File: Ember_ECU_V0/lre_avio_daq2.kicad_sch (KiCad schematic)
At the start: 64 parts, among them IC1 AS5600-ASOT, IC2 AS5600-ASOT, J1 Screw_Terminal_01x02, J2 Conn_01x04, U1 STM32F411CEUx, U2 HX711, U3 SN65HVD230, U4 MPXA6115A, U5 MPXA6115A, U6 MPXA6115A, U7 MAX31856, U8 MAX31856, U9 MAX31856, Y1 8 MHz

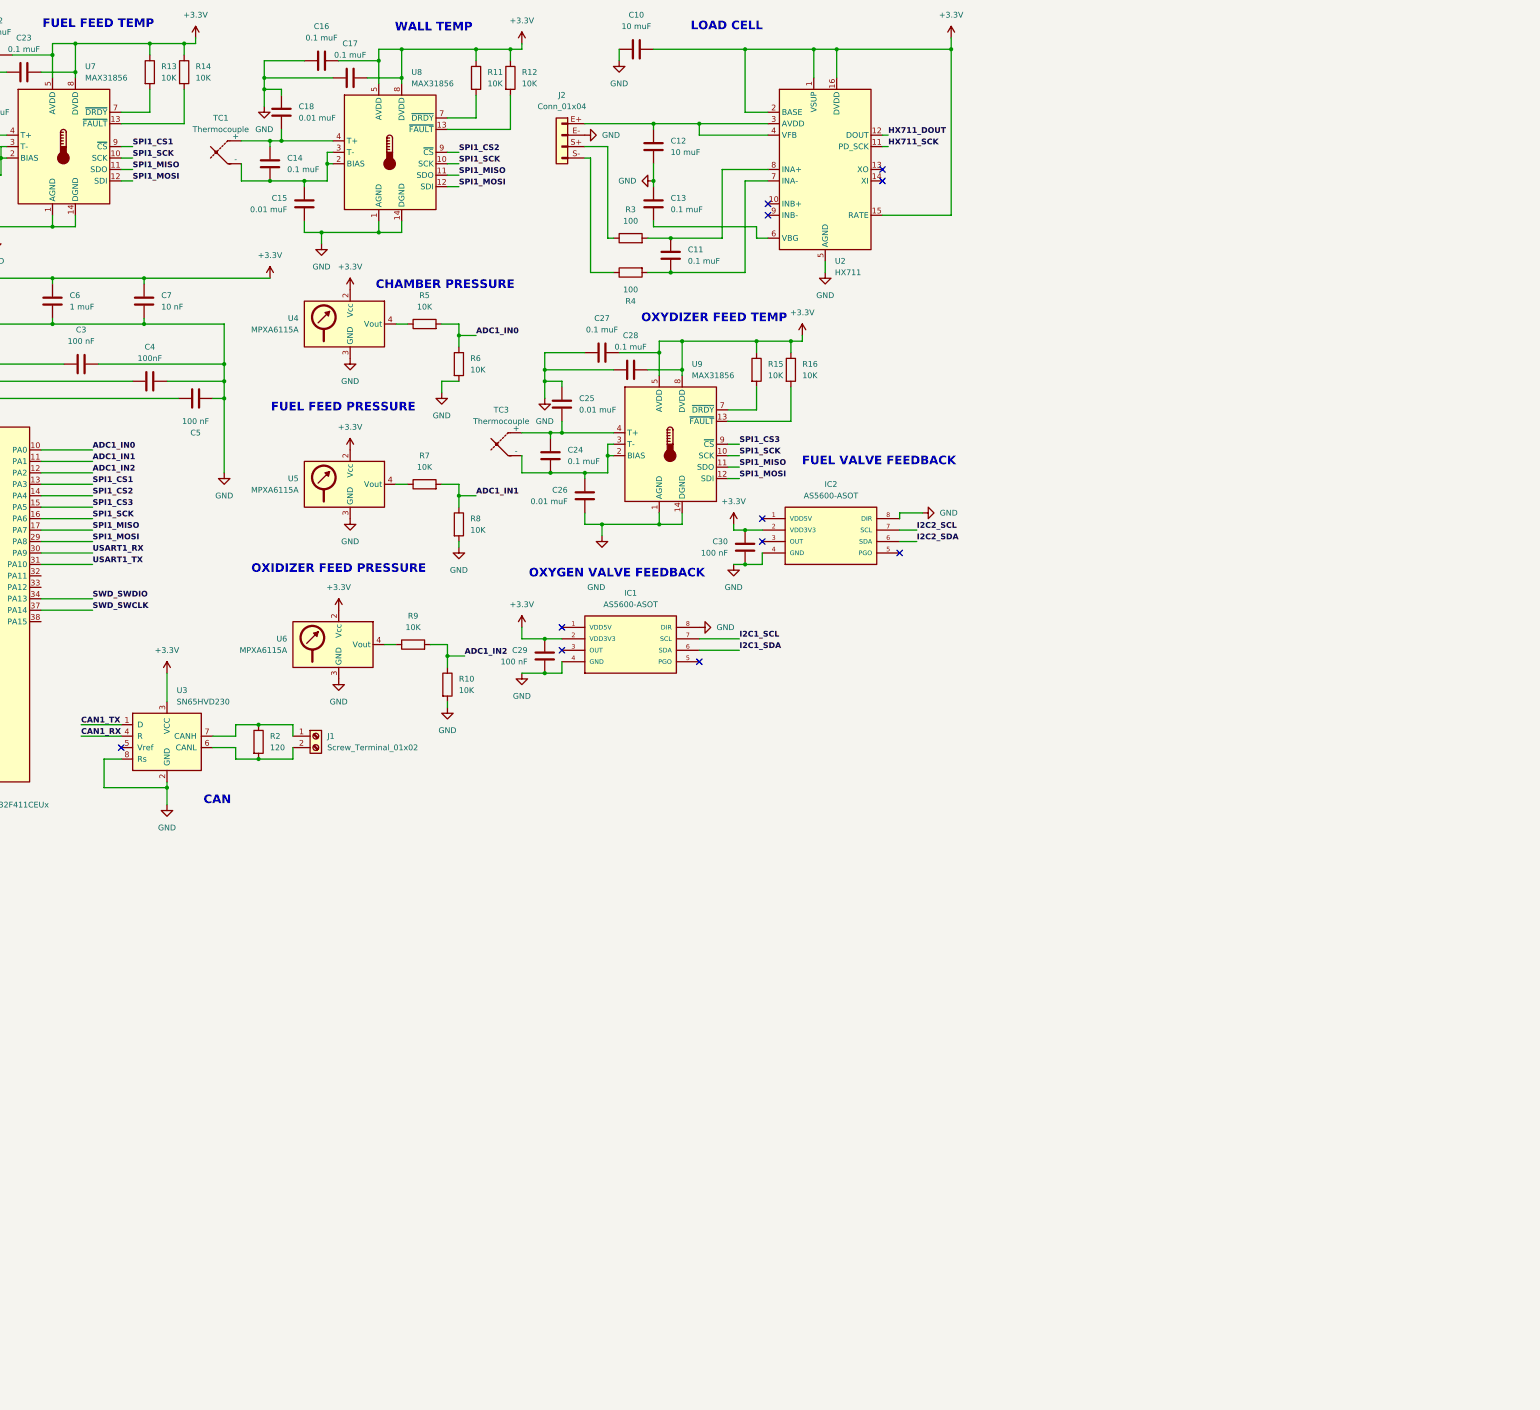
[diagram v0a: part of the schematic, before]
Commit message: corrections on ECU
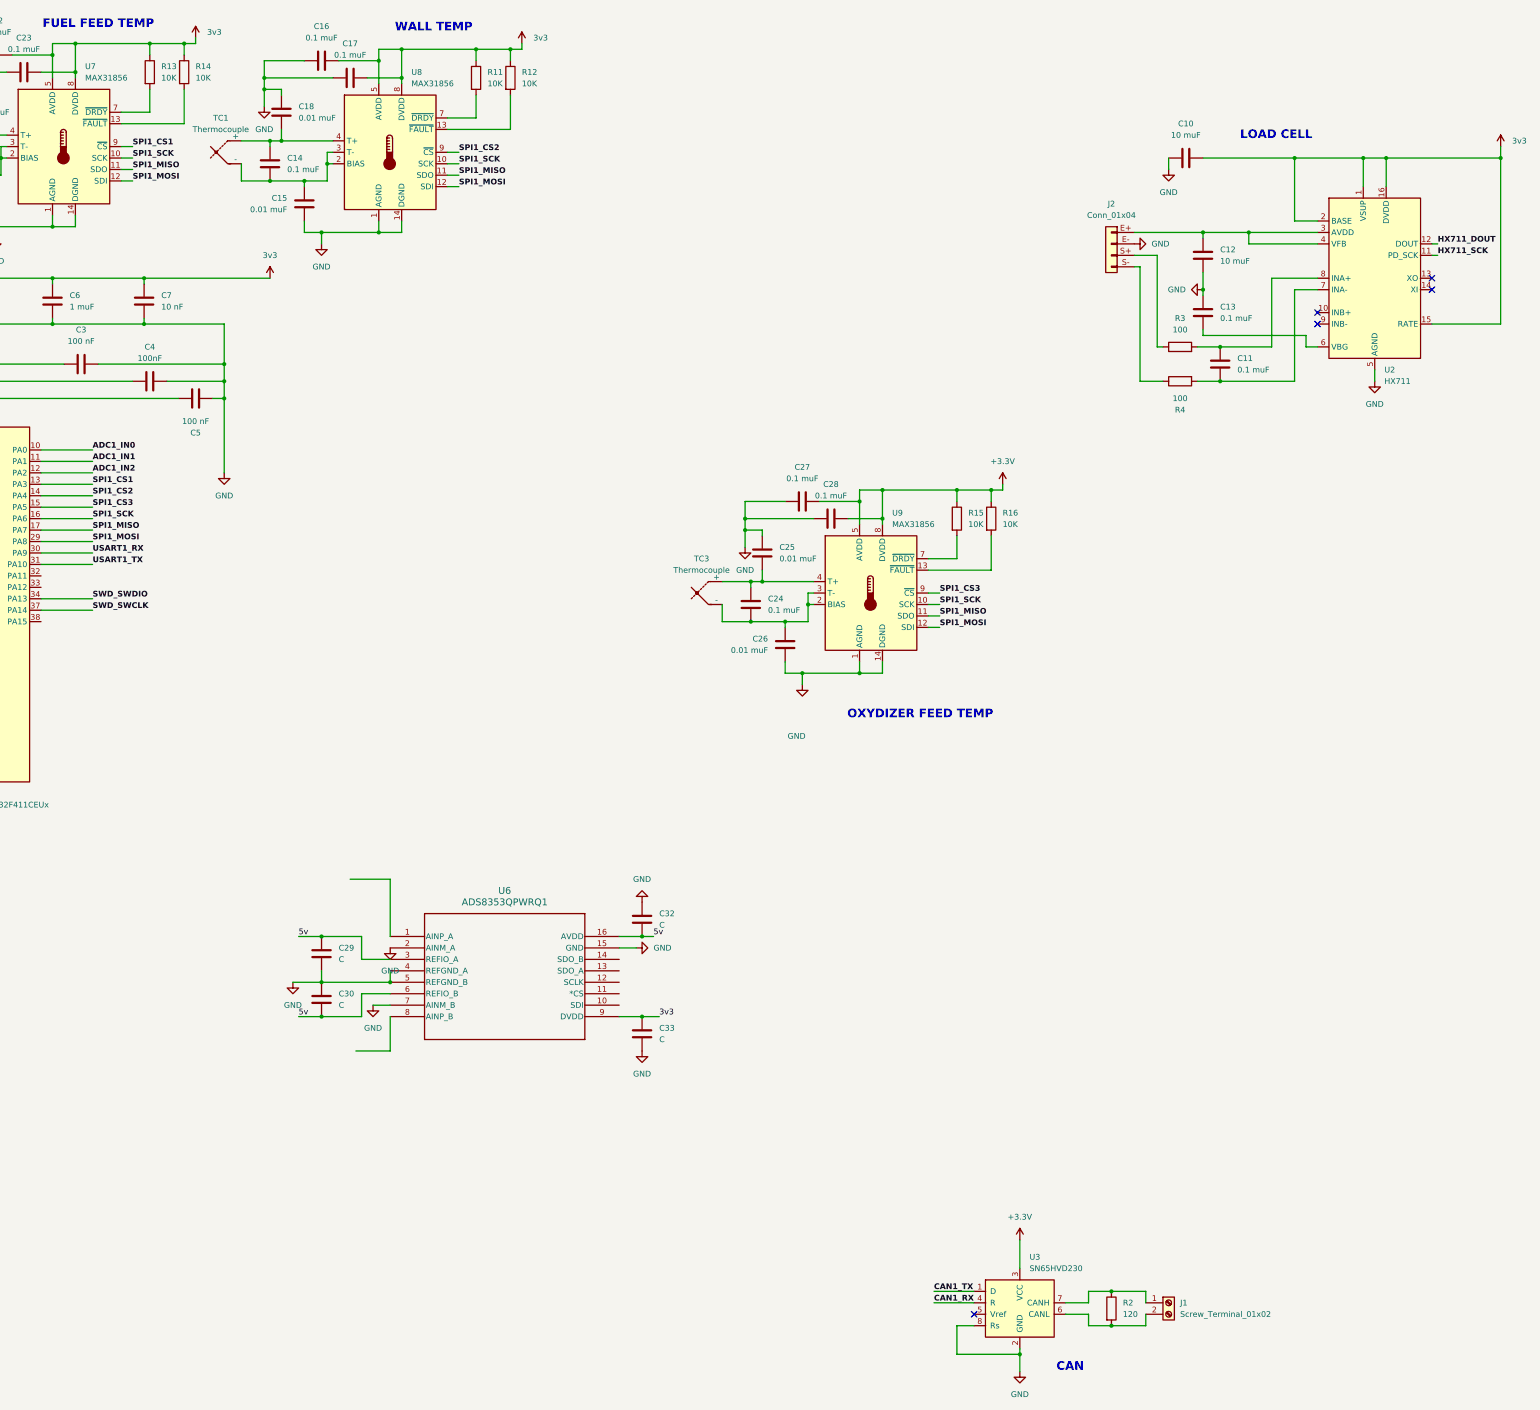
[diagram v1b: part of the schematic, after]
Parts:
- removed IC1, IC2: AS5600-ASOT, AS5600-ASOT:SOIC127P600X175-8N, symbol AS5600-ASOT:AS5600-ASOT
- removed R10, R5, R6, R7, R8, R9: 10K, symbol Device:R
- removed U4, U5, U6: MPXA6115A, symbol Sensor_Pressure:MPXA6115A
- added C32, C33: C, Capacitor_SMD:C_0201_0603Metric, symbol Device:C
- added U6: ADS8353QPWRQ1, ads8353:TSSOP16_PW_TEX-L, symbol ads8353:ADS8353QPWRQ1
- C29: value 100 nF -> C; footprint (none) -> Capacitor_SMD:C_0201_0603Metric
- C30: value 100 nF -> C
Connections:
- net +3.3V: no longer C1.1, C10.1, C10.2, C12.2, C13.1, C15.2, C16.1, C16.2, C17.1, C17.2, C18.1, C2.1, C20.1, C21.2, C22.1, C22.2, C23.1, C23.2, C25.1, C26.2, C27.1, C28.1, C29.1, C29.2, C3.2, C30.1, C30.2, C31.2, C4.2, C5.2, C6.1, C6.2, C7.1, C7.2, C8.1, C9.1, J2.E- (Pin_2), R1.1, R11.1, R12.1, R13.1, R14.1, U1.23 (VSS), U1.35 (VSS), U1.47 (VSS), U1.49 (VSS), U1.8 (VSSA), U1.9 (VDDA), U2.1 (VSUP), U2.15 (RATE), U2.16 (DVDD), U2.2 (BASE), U2.5 (AGND), U3.2 (GND), U3.8 (Rs), U7.1 (AGND), U7.14 (DGND), U7.5 (AVDD), U7.8 (DVDD), U8.1 (AGND), U8.14 (DGND), U8.5 (AVDD), U8.8 (DVDD), U9.1 (AGND), U9.14 (DGND)
- new net 3v3: C1.1, C10.1, C10.2, C12.2, C13.1, C15.2, C16.1, C16.2, C17.1, C17.2, C18.1, C2.1, C20.1, C21.2, C22.1, C22.2, C23.1, C23.2, C25.1, C26.2, C27.1, C28.1, C29.1, C3.2, C30.1, C31.2, C32.1, C33.1, C33.2, C4.2, C5.2, C6.1, C6.2, C7.1, C7.2, C8.1, C9.1, J2.E- (Pin_2), R1.1, R11.1, R12.1, R13.1, R14.1, U1.23 (VSS), U1.35 (VSS), U1.47 (VSS), U1.49 (VSS), U1.8 (VSSA), U1.9 (VDDA), U2.1 (VSUP), U2.15 (RATE), U2.16 (DVDD), U2.2 (BASE), U2.5 (AGND), U3.2 (GND), U3.8 (Rs), U6.15 (GND), U6.2 (AINM_A), U6.4 (REFGND_A), U6.5 (REFGND_B), U6.7 (AINM_B), U6.9 (DVDD), U7.1 (AGND), U7.14 (DGND), U7.5 (AVDD), U7.8 (DVDD), U8.1 (AGND), U8.14 (DGND), U8.5 (AVDD), U8.8 (DVDD), U9.1 (AGND), U9.14 (DGND)
- new net 5v: C29.2, C30.2, C32.2, U6.16 (AVDD), U6.3 (REFIO_A), U6.6 (REFIO_B)
- no-connect marks 11 -> 5
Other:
- note removed: "CHAMBER PRESSURE"
- note removed: "FUEL FEED PRESSURE"
- note removed: "FUEL VALVE FEEDBACK"
- note removed: "OXIDIZER FEED PRESSURE"
- note removed: "OXYGEN VALVE FEEDBACK"
- moved on the sheet: C10, C11, C12, C13, C24, C25, C26, C27, C28, J1, J2, R15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

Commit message: Updated lre_avio_daq2 schematic and project files
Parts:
- removed U1: STM32F411CEUx, Package_DFN_QFN:QFN-48-1EP_7x7mm_P0.5mm_EP5.6x5.6mm, symbol MCU_ST_STM32F4:STM32F411CEUx
- added C34, C36, C37, C38, C40, C41: C, Capacitor_SMD:C_0201_0603Metric, symbol Device:C
- added C35, C39: C, symbol Device:C
- added C42: 10 nF, symbol Device:C
- added C43, C46, C48, C49, C52: 1 muF, symbol Device:C
- added C44, C45, C47, C50, C51: 100 nF, symbol Device:C
- added J3: Conn_01x02_Socket, symbol Connector:Conn_01x02_Socket
- added J4: DB25_Socket, symbol Connector:DB25_Socket
- added U1, U5: AMS1117-5.0, Package_TO_SOT_SMD:SOT-223-3_TabPin2, symbol Regulator_Linear:AMS1117-5.0
- added U10, U11: ADS8353QPWRQ1, ads8353:TSSOP16_PW_TEX-L, symbol ads8353:ADS8353QPWRQ1
- added U4: STM32F411VETx, Package_QFP:LQFP-100_14x14mm_P0.5mm, symbol MCU_ST_STM32F4:STM32F411VETx
- C1: value 100 nF -> 4.7 muF
- C2: value 1 muF -> 4.7 muF
- C31: value 4.7 muF -> 100 nF
- C4: value 100nF -> 100 nF
- C6: value 1 muF -> 100 nF
- C7: value 10 nF -> 100 nF
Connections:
- net +3.3V: no longer C2.2, C3.1, C4.1, C5.1, U3.3 (VCC)
- net 3v3: now also C3.1, C31.1, C4.1, C5.1, U3.3 (VCC), C37.1, C41.1, C42.1, C43.1, C51.1, C52.1, U10.9 (DVDD), U11.9 (DVDD), U4.100 (VDD), U4.11 (VDD), U4.19 (VDD), U4.28 (VDD), U4.50 (VDD), U4.6 (VBAT), U4.75 (VDD); no longer C1.1, C10.1, C12.2, C13.1, C15.2, C16.1, C17.1, C18.1, C2.1, C20.1, C21.2, C22.1, C23.1, C25.1, C26.2, C27.1, C28.1, C29.1, C3.2, C30.1, C31.2, C32.1, C33.2, C4.2, C5.2, C6.2, C7.2, C8.1, C9.1, J2.E- (Pin_2), R1.1, U2.5 (AGND), U3.2 (GND), U3.8 (Rs), U6.15 (GND), U6.2 (AINM_A), U6.4 (REFGND_A), U6.5 (REFGND_B), U6.7 (AINM_B), U7.1 (AGND), U7.14 (DGND), U8.1 (AGND), U8.14 (DGND), U9.1 (AGND), U9.14 (DGND)
- net 5v: now also C34.2, C35.2, C36.2, C38.2, C39.2, C40.2, C47.1, C48.1, C49.1, C50.1, U10.16 (AVDD), U10.3 (REFIO_A), U10.6 (REFIO_B), U11.16 (AVDD), U11.3 (REFIO_A), U11.6 (REFIO_B)
- net HX711_DOUT: now also U4.35 (PB0)
- net HX711_SCK: now also U4.36 (PB1)
- net OSC_IN: now also U4.12 (PH0)
- net OSC_OUT: now also U4.13 (PH1)
- net SPI2_MISO: now also U6.12 (SCLK), U4.53 (PB14)
- net SPI2_MOSI: now also U6.10 (SDI), U4.54 (PB15)
- net SPI2_SCK: now also U6.13 (SDO_A), U4.52 (PB13)
- net at R1.2: now also U4.94 (BOOT0)
- net GND: now reaches C1.2
- net GND: now also C10.1, C12.2, C13.1, C15.2, C16.1, C17.1, C18.1, C2.2, C20.1, C21.2, C22.1, C23.1, C25.1, C26.2, C27.1, C28.1, C29.1, C3.2, C30.1, C31.2, C32.1, C33.2, C4.2, C5.2, C6.2, C7.2, C8.1, C9.1, J2.E- (Pin_2), R1.1, U2.5 (AGND), U3.2 (GND), U3.8 (Rs), U6.15 (GND), U6.2 (AINM_A), U6.4 (REFGND_A), U6.5 (REFGND_B), U6.7 (AINM_B), U7.1 (AGND), U7.14 (DGND), U8.1 (AGND), U8.14 (DGND), U9.1 (AGND), U9.14 (DGND), C34.1, C35.1, C36.1, C37.2, C38.1, C39.1, C40.1, C41.2, C42.2, C43.2, C44.1, J3.2 (Pin_2), J4.13, J4.21 (P21), J4.22 (P22), J4.23 (P23), J4.24 (P24), J4.25 (P25), U1.1 (GND), U10.15 (GND), U10.2 (AINM_A), U10.4 (REFGND_A), U10.5 (REFGND_B), U10.7 (AINM_B), U11.15 (GND), U11.2 (AINM_A), U11.4 (REFGND_A), U11.5 (REFGND_B), U11.7 (AINM_B), U4.10 (VSS), U4.20 (VSSA), U4.21 (VREF+), U4.27 (VSS), U4.49 (VSS), U4.74 (VSS), U4.99 (VSS), U5.1 (GND)
- net ADS1_CS: now reaches U6.11 (*CS)
- new net: C47.2, C48.2, U1.2 (VO)
- new net: C45.2, C46.2, U1.3 (VI)
- new net: C49.2, C50.2, U5.3 (VI)
- new net: C2.1, U4.48 (VCAP1)
- new net: C44.2, U4.14 (NRST)
- new net: C1.1, U4.73 (VCAP2)
- new net: C51.2, C52.2, U5.2 (VO)
- new net 7v4: C45.1, C46.1, J3.1 (Pin_1), J4.16 (P16), J4.17 (P17), J4.18 (P18), J4.19 (P19), J4.20 (P20)
- new net ADC1_CS: U4.51 (PB12)
- new net ADC2_CS: U4.29 (PA4)
- new net ADC3_CS: U4.3 (PE4)
- new net ADS2_CS: U10.11 (*CS)
- new net ADS3_CS: U11.11 (*CS)
- new net PWM_SERVO1: J4.1, J4.2, U4.40 (PE9)
- new net PWM_SERVO2: J4.3, J4.4, U4.42 (PE11)
- new net PWM_SERVO3: J4.5, J4.6, U4.44 (PE13)
- new net PWM_SERVO4: J4.7, J4.8, U4.45 (PE14)
- new net PWM_SERVO5: J4.10, J4.9, U4.61 (PD14)
- new net PWM_SERVO6: J4.11, J4.12, U4.62 (PD15)
- new net PWM_SERVO7: J4.14 (P14), J4.15 (P15), U4.63 (PC6)
- new net SPI3_MISO: U10.12 (SCLK), U4.31 (PA6)
- new net SPI3_MOSI: U10.10 (SDI), U4.32 (PA7)
- new net SPI3_SCK: U10.13 (SDO_A), U4.30 (PA5)
- new net SPI4_MISO: U11.12 (SCLK), U4.4 (PE5)
- new net SPI4_MOSI: U11.10 (SDI), U4.5 (PE6)
- new net SPI4_SCK: U11.13 (SDO_A), U4.1 (PE2)
- no-connect marks 5 -> 8
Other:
- note removed: "MCU"
- moved on the sheet: C10, C11, C12, C13, C24, C25, C26, C27, C28, C29, C30, C32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

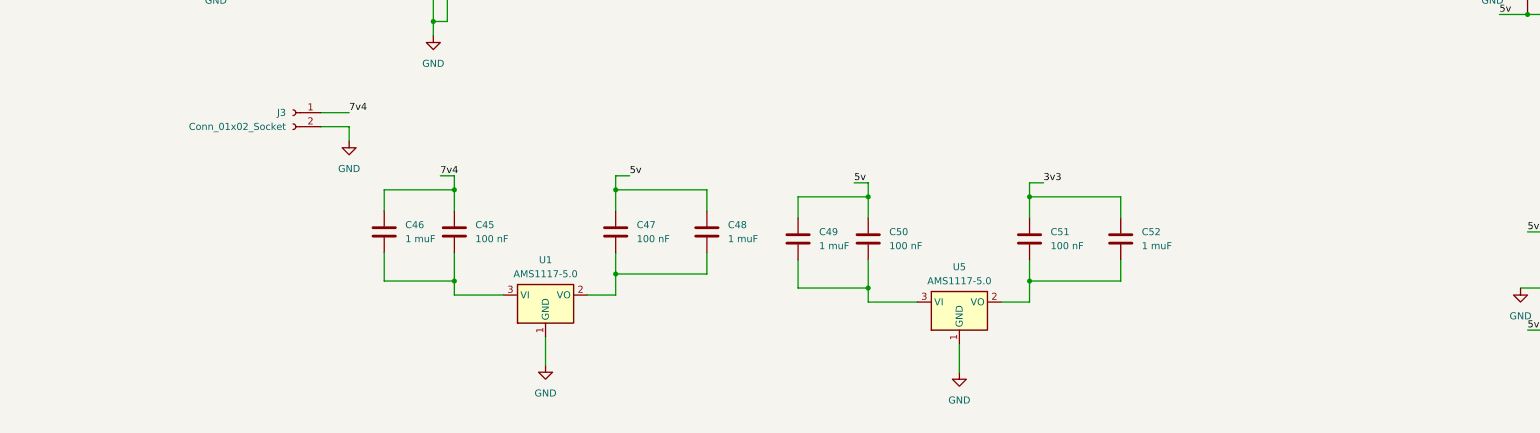
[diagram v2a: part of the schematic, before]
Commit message: corrected the LDO, added xt60pw and schottky diode
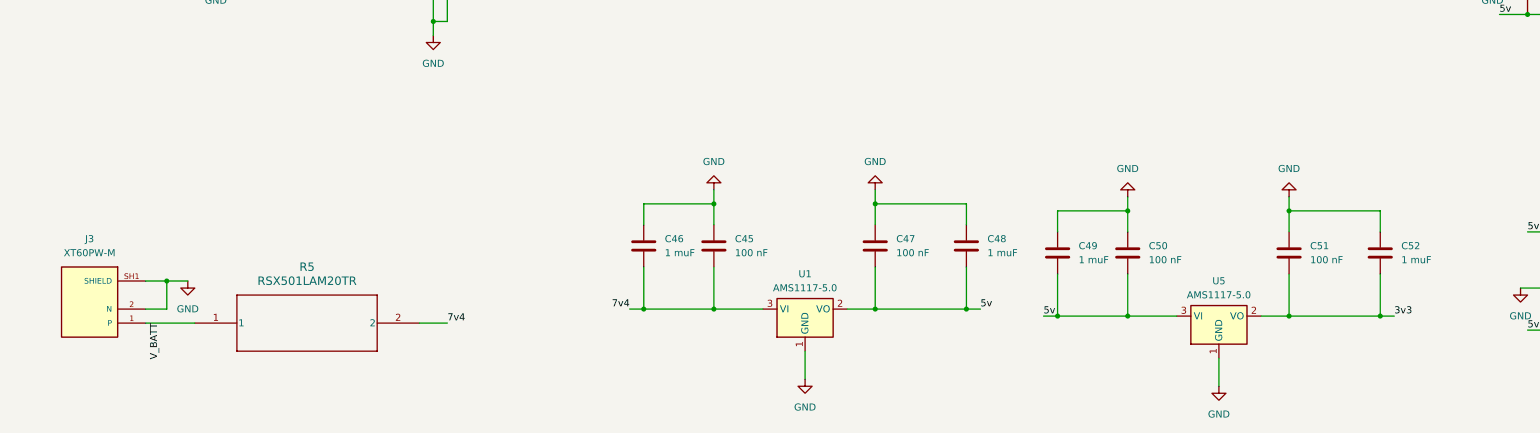
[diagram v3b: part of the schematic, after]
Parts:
- removed J3: Conn_01x02_Socket, symbol Connector:Conn_01x02_Socket
- added J3: XT60PW-M, XT60PW-M:AMASS_XT60PW-M, symbol XT60PW-M:XT60PW-M
- added R5: RSX501LAM20TR, RSX501LAM20TR:DIO_RB050LAM_ROM-L, symbol RSX501LAM20TR:RSX501LAM20TR
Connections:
- net 3v3: now also C51.2, C52.2, U5.2 (VO); no longer C51.1, C52.1
- net 5v: now also C47.2, C48.2, C49.2, C50.2, U1.2 (VO), U5.3 (VI); no longer C47.1, C48.1, C49.1, C50.1
- net 7v4: now also C45.2, C46.2, U1.3 (VI), R5.2; no longer C45.1, C46.1
- net GND: now also C45.1, C46.1, C47.1, C48.1, C49.1, C50.1, C51.1, C52.1, J3.2 (N), J3.SH1 (SHIELD), J3.SH2 (SHIELD)
- new net V_BATT: J3.1 (P), R5.1
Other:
- moved on the sheet: C45, C46, C47, C48, C49, C50, C51, C52, U1, U5

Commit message: Updated lre_avio_daq2 schematic and project files
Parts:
- removed C31, C4, C44, C5, C6, C7: 100 nF, symbol Device:C
- removed C42: 10 nF, symbol Device:C
- removed C43: 1 muF, symbol Device:C
- removed U4: STM32F411VETx, Package_QFP:LQFP-100_14x14mm_P0.5mm, symbol MCU_ST_STM32F4:STM32F411VETx
- added C53, C54, C55, C56, C57, C58, C61: 100 nF, symbol Device:C
- added C59: 10 nF, symbol Device:C
- added C60: 1 muF, symbol Device:C
- added C62, C63: 4.7 muF, symbol Device:C
- added J5, J6, J7: Conn_01x03_Socket, symbol Connector:Conn_01x03_Socket
- added R6: 10K, symbol Device:R
- added R7, R8: 100, symbol Device:R
- added U12: STM32F412VGTx, Package_QFP:LQFP-100_14x14mm_P0.5mm, symbol MCU_ST_STM32F4:STM32F412VGTx
- C1, C2: value 4.7 muF -> 1nF
- C3: value 100 nF -> 1nF
- R1: value 10K -> 100
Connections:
- net 3v3: now also C53.1, C54.1, C55.1, C56.1, C57.1, C58.1, C59.1, C60.1, U12.100 (VDD), U12.11 (VDD), U12.19 (VDD), U12.28 (VDD), U12.50 (VDD), U12.6 (VBAT), U12.75 (VDD); no longer C3.1
- net 5v: now also J5.1 (Pin_1), J6.1 (Pin_1), J7.1 (Pin_1)
- net ADS1_CS: now also U12.51 (PB12)
- net ADS2_CS: now also U12.77 (PA15)
- net ADS3_CS: now also U12.3 (PE4)
- net CAN1_RX: now also U12.70 (PA11)
- net CAN1_TX: now also U12.71 (PA12)
- net GND: now also C53.2, C54.2, C55.2, C56.2, C57.2, C58.2, C59.2, C60.2, C61.1, C62.2, C63.2, J5.3 (Pin_3), J6.3 (Pin_3), J7.3 (Pin_3), R6.1, U12.10 (VSS), U12.20 (VSSA), U12.21 (VREF+), U12.27 (VSS), U12.49 (VSS), U12.74 (VSS), U12.99 (VSS); no longer R1.1
- net HX711_DOUT: now also U12.18 (PC3)
- net HX711_SCK: now also U12.33 (PC4)
- net OSC_IN: now also U12.12 (PH0)
- net OSC_OUT: now also U12.13 (PH1)
- net PWM_SERVO1: now also U12.67 (PA8)
- net PWM_SERVO2: now also U12.95 (PB8)
- net PWM_SERVO3: now also U12.96 (PB9)
- net PWM_SERVO4: now also U12.63 (PC6)
- net PWM_SERVO5: now also U12.64 (PC7)
- net PWM_SERVO6: now also U12.65 (PC8)
- net PWM_SERVO7: now also U12.66 (PC9)
- net SPI1_MISO: now also U12.31 (PA6)
- net SPI1_MOSI: now also U12.32 (PA7)
- net SPI1_SCK: now also U12.30 (PA5)
- net SPI2_MISO: now also U12.53 (PB14)
- net SPI2_MOSI: now also U12.54 (PB15)
- net SPI2_SCK: now also U12.52 (PB13)
- net SPI3_MISO: now also U12.79 (PC11)
- net SPI3_MOSI: now also U12.80 (PC12)
- net SPI3_SCK: now also U12.78 (PC10)
- net SPI4_MISO: now also U12.5 (PE6)
- net SPI4_MOSI: now also U12.38 (PE7)
- net SPI4_SCK: now also U12.1 (PE2)
- net at U11.1 (AINP_A): now also J7.2 (Pin_2), R8.1
- net at R1.2: now also C1.1, U6.1 (AINP_A)
- net at C2.1: now also R7.2
- net at U10.1 (AINP_A): now also J6.2 (Pin_2), R7.1
- new net: J5.2 (Pin_2), R1.1
- new net: C62.1, U12.48 (VCAP_1)
- new net: C61.2, U12.14 (NRST)
- new net: C63.1, U12.73 (VCAP_2)
- new net: R6.2, U12.94 (BOOT0)
- new net: C3.1, R8.2
- new net TC1_CS: U12.29 (PA4)
- new net TC2_CS: U12.35 (PB0)
- new net TC3_CS: U12.36 (PB1)
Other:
- moved on the sheet: C38, C39, C40, C41, U11

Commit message: commit
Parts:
- added C4, C5, C6: 1nF, symbol Device:C
- added D1: 1N914, Diode_THT:D_DO-35_SOD27_P7.62mm_Horizontal, symbol Diode:1N914
- added J10, J8, J9: Conn_01x03_Socket, symbol Connector:Conn_01x03_Socket
- added J11: DROGUE, OSTTA020161:ONSHORE_OSTTA020161, symbol OSTTA020161:OSTTA020161
- added Q1: 2N3904, Package_TO_SOT_THT:TO-92_Inline, symbol Transistor_BJT:2N3904
- added R10, R17, R9: 100, symbol Device:R
- added R18, R20: 150K, symbol Device:R
- added R19, R21: 100K, symbol Device:R
- added R22: 33K, symbol Device:R
- added R23: 1K, symbol Device:R
- added SW1, SW2: SW_Nidec_CAS-120A1, Button_Switch_SMD:Nidec_Copal_CAS-120A, symbol Switch:SW_Nidec_CAS-120A1
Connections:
- net 3v3: now also SW1.1 (C), SW2.1 (C)
- net 5v: now also J10.1 (Pin_1), J8.1 (Pin_1), J9.1 (Pin_1)
- net 7v4: now also D1.2 (A), SW1.2 (B)
- net GND: now also C4.2, C5.2, C6.2, J10.3 (Pin_3), J8.3 (Pin_3), J9.3 (Pin_3), Q1.1 (E), R19.2, R21.2, R22.2, SW1.3 (A), SW2.3 (A)
- net at J7.2 (Pin_2), R8.1: no longer U11.1 (AINP_A)
- net at U11.8 (AINP_B): now also C6.1, R17.2
- net BATTERY_MON: now reaches U12.15 (PC0)
- net BATTERY_MON: now also R18.2, R19.1
- net ARM: now reaches U12.16 (PC1)
- net ARM: now also R20.2, R21.1
- net Conn: now reaches U12.17 (PC2)
- net Conn: now also R23.2
- net at C2.1, R7.2: now also U10.1 (AINP_A)
- net at J6.2 (Pin_2), R7.1: no longer U10.1 (AINP_A)
- net at C3.1, R8.2: now also U11.1 (AINP_A)
- net at U10.8 (AINP_B): now also C5.1, R10.2
- net at U6.8 (AINP_B): now also C4.1, R9.2
- new net: D1.1 (K), J11.1, R18.1, R20.1, SW2.2 (B)
- new net: J8.2 (Pin_2), R9.1
- new net: J10.2 (Pin_2), R17.1
- new net: Q1.2 (B), R22.1, R23.1
- new net: J11.2, Q1.3 (C)
- new net: J9.2 (Pin_2), R10.1
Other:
- moved on the sheet: C45, C46, C47, C48, C49, C50, C51, C52, U1, U5

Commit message: commit
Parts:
- removed D1: 1N914, Diode_THT:D_DO-35_SOD27_P7.62mm_Horizontal, symbol Diode:1N914
- removed J11: DROGUE, OSTTA020161:ONSHORE_OSTTA020161, symbol OSTTA020161:OSTTA020161
- removed Q1: 2N3904, Package_TO_SOT_THT:TO-92_Inline, symbol Transistor_BJT:2N3904
- removed R22: 33K, symbol Device:R
- removed R23: 1K, symbol Device:R
- removed SW1, SW2: SW_Nidec_CAS-120A1, Button_Switch_SMD:Nidec_Copal_CAS-120A, symbol Switch:SW_Nidec_CAS-120A1
- added J12, J13, J14: XT30PW-F, CONN_XT30PW-F_AMA, symbol 2026-08-03_13-16-17:XT30PW-F
- added Q2: SISA96DN-T1, SISA96DN-T1-GE3:SIS862DNT1GE3, symbol SISA96DN-T1-GE3:SISA96DN-T1-GE3
- added R28: 33k, microbuilder:0603, symbol microbuilder:RESISTOR0603
- added R29: 1k, microbuilder:0603, symbol microbuilder:RESISTOR0603
- added SW1: SW_SPDT, symbol Switch:SW_SPDT
- added TP2, TP3: TestPoint_Probe, TestPoint:TestPoint_Pad_D1.5mm, symbol Connector:TestPoint_Probe
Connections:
- net 3v3: now also SW1.3 (C)
- net 7v4: now also R18.1, R20.1, J12.1, J12.2, J13.1, J13.2, J14.1, J14.2, Q2.10 (D_6), Q2.11 (D_7), Q2.5 (D_1), Q2.6 (D_2), Q2.7 (D_3), Q2.8 (D_4), Q2.9 (D_5)
- net Conn: now also R29.1
- net GND: now also Q2.1 (S_1), Q2.2 (S_2), Q2.3 (S_3), R28.2, SW1.1 (A), TP3.1; no longer C61.1, R6.1
- new net: Q2.4 (G), R28.1, R29.2
- new net: C61.1, TP2.1
- new net: R6.1, SW1.2 (B)
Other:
- moved on the sheet: R20, R21
